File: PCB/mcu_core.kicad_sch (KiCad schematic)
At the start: 11 parts

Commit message: task: write matched LCSC part numbers into the schematic
Adds scripts/apply_lcsc_fields.py, which clones each symbol's existing
Manufacturer_Part_Number property (same indentation/effects) into a new
'LCSC' field with the matched code -- the field name the Fabrication
Toolkit plugin already installed in this repo recognizes for JLCPCB BOM
matching.

Applied the 31 confirmed matches from jlc_match.py across all sheets
(68 individual references). C_BUCK_OUT1 and R_ISET1 are left without an
LCSC field -- JLC doesn't stock those exact Yageo part numbers, to be
sorted out separately.

Verified: kicad-cli sch export bom round-trips every LCSC value
correctly, and ERC reports 0 violations.

Also switched jlc_match.py's BOM export to unranged references so each
match maps cleanly to individual schematic symbols.

Co-Authored-By: Claude Sonnet 5 <noreply@anthropic.com>
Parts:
- C_3V3_1: LCSC (none) -> C2936601
- C_3V3_2: LCSC (none) -> C131394
- C_3V3_3: LCSC (none) -> C106223
- R_BOOT_PU1, R_EN_PU1: LCSC (none) -> C60490
- R_USB_DM1, R_USB_DP1: LCSC (none) -> C138021
- R_VSYS1: LCSC (none) -> C114763
- R_VSYS2: LCSC (none) -> C60491
- SW_BOOT1: LCSC (none) -> C2915174
- U_MCU1: LCSC (none) -> C2913198
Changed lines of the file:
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@@
+			)
+		)
+		(property "LCSC" "C2936601"
+			(at 0 0 0)
+			(hide yes)
+			(show_name no)
+			(do_not_autoplace no)
+			(effects
+				(font
+					(size 1.27 1.27)
+				)
 			)
 		)
@@
 			)
 		)
+		(property "LCSC" "C2913198"
+			(at 0 0 0)
+			(hide yes)
+			(show_name no)
+			(do_not_autoplace no)
+			(effects
+				(font
+					(size 1.27 1.27)
+				)
+			)
+		)
 		(pin "1"
 		)
@@
 			)
 		)
+		(property "LCSC" "C60490"
+			(at 0 0 0)
+			(hide yes)
+			(show_name no)
+			(do_not_autoplace no)
+			(effects
+				(font
+					(size 1.27 1.27)
+				)
+			)
+		)
 		(pin "1"
 		)
@@
 			)
 		)
+		(property "LCSC" "C106223"
+			(at 0 0 0)
+			(hide yes)
+			(show_name no)
+			(do_not_autoplace no)
+			(effects
+				(font
+					(size 1.27 1.27)
+				)
+			)
+		)
 		(pin "1"
 		)
@@
 			)
 		)
+		(property "LCSC" "C60490"
+			(at 0 0 0)
+			(hide yes)
+			(show_name no)
+			(do_not_autoplace no)
+			(effects
+				(font
+					(size 1.27 1.27)
+				)
+			)
+		)
 		(pin "1"
 		)
@@
 			)
 		)
+		(property "LCSC" "C114763"
+			(at 0 0 0)
+			(hide yes)
+			(show_name no)
+			(do_not_autoplace no)
+			(effects
+				(font
+					(size 1.27 1.27)
+				)
+			)
+		)
 		(pin "1"
 		)
@@
 			)
 		)
+		(property "LCSC" "C2915174"
+			(at 0 0 0)
+			(hide yes)
+			(show_name no)
+			(do_not_autoplace no)
+			(effects
+				(font
+					(size 1.27 1.27)
+				)
+			)
+		)
 		(property "MF" "Panasonic"
 			(at 0 0 0)
@@
 			)
 		)
+		(property "LCSC" "C138021"
+			(at 0 0 0)
+			(hide yes)
+			(show_name no)
+			(do_not_autoplace no)
+			(effects
+				(font
+					(size 1.27 1.27)
+				)
+			)
+		)
 		(pin "1"
 		)
@@
 			)
 		)
+		(property "LCSC" "C60491"
+			(at 0 0 0)
+			(hide yes)
+			(show_name no)
+			(do_not_autoplace no)
+			(effects
+				(font
+					(size 1.27 1.27)
+				)
+			)
+		)
 		(pin "1"
 		)
@@
 			)
 		)
+		(property "LCSC" "C131394"
+			(at 0 0 0)
+			(hide yes)
+			(show_name no)
+			(do_not_autoplace no)
+			(effects
+				(font
+					(size 1.27 1.27)
+				)
+			)
+		)
 		(pin "1"
 		)
@@
 			(at 0 0 0)
 			(hide yes)
+			(show_name no)
+			(do_not_autoplace no)
+			(effects
+				(font
+					(size 1.27 1.27)
+				)
+			)
+		)
+		(property "LCSC" "C138021"
+			(at 0 0 0)
+			(hide yes)

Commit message: task: alert on Basic-library alternatives during JLC part matching (#33)
* task: alert on Basic-library alternatives during JLC part matching

JLC's "Extended" library carries a per-unique-part setup fee on top of
unit price; "Basic" doesn't. That fee doesn't amortize well on a board
with many distinct low-quantity parts -- confirmed the hard way: our
first real JLCPCB assembly quote came back at $333.84 vs PCBWay's
~$190 for the same order, and all 33 of our matched parts were
Extended.

jlc_match.py now does a secondary search for a same-value/same-package
Basic-library part whenever the real match lands on Extended, and
flags it in the report (new BasicAlt column + a Status alert) rather
than silently leaving it. On the current board this surfaces 11
plausible Basic-library swaps (common resistor/cap values, and the
generic 1N4148W diode and 2N7002 MOSFET, which are industry-standard
parts many brands stock identically).

This is alert-only, same as the rest of this script -- it doesn't
touch the schematic. Spot-checked 4 of the 11 suggestions directly
against JLC's catalog to confirm value/package actually match, not
just a keyword hit.

Co-Authored-By: Claude Sonnet 5 <noreply@anthropic.com>

* fix: two correctness bugs in Basic-library alternative matching

1. find_basic_alternative() trusted the raw keyword-search hit without
   verifying the candidate's actual value -- JLC's fuzzy full-text search
   can return a wrong-value part that just shares digits (e.g. searching
   "100 0402" surfaced a 1kΩ resistor, EIA code "1001", as a false match
   for a 100Ω part). Now parses and compares the actual numeric value
   (with unit) before accepting a candidate; falls back to exact
   model-name matching for non-numeric values (generic diode/transistor
   part families like "1N4148W", "2N7002").

2. The new value parser's regex required the unit to be the first
   character of the string, but JLC resistor descriptions carry a
   Chinese prefix ("厚膜电阻 10kΩ ±1%" = "thi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
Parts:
- C_3V3_1: LCSC C2936601 -> C19702; MF Yageo -> Samsung Electro-Mechanics; Manufacturer_Part_Number CC0603KRX5R7BB106 -> CL10A106KP8NNNC
- C_3V3_2: LCSC C131394 -> C1525; MF Yageo -> Samsung Electro-Mechanics; Manufacturer_Part_Number CC0402KRX7R9BB104 -> CL05B104KO5NNNC
- R_BOOT_PU1, R_EN_PU1: LCSC C60490 -> C25744; MF Yageo -> UNI-ROYAL(Uniroyal Elec); Manufacturer_Part_Number RC0402FR-0710KL -> 0402WGF1002TCE
- R_VSYS1: LCSC C114763 -> C25764; MF Yageo -> UNI-ROYAL(Uniroyal Elec); Manufacturer_Part_Number RC0402FR-07200KL -> 0402WGF2003TCE
- R_VSYS2: LCSC C60491 -> C25741; MF Yageo -> UNI-ROYAL(Uniroyal Elec); Manufacturer_Part_Number RC0402FR-07100KL -> 0402WGF1003TCE
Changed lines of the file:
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@@
 			)
 		)
-		(property "MF" "Yageo"
-			(at 0 0 0)
-			(hide yes)
-			(show_name no)
-			(do_not_autoplace no)
-			(effects
-				(font
-					(size 1.27 1.27)
-				)
-			)
-		)
-		(property "Manufacturer_Part_Number" "CC0603KRX5R7BB106"
-			(at 0 0 0)
-			(hide yes)
-			(show_name no)
-			(do_not_autoplace no)
-			(effects
-				(font
-					(size 1.27 1.27)
-				)
-			)
-		)
-		(property "LCSC" "C2936601"
+		(property "MF" "Samsung Electro-Mechanics"
+			(at 0 0 0)
+			(hide yes)
+			(show_name no)
+			(do_not_autoplace no)
+			(effects
+				(font
+					(size 1.27 1.27)
+				)
+			)
+		)
+		(property "Manufacturer_Part_Number" "CL10A106KP8NNNC"
+			(at 0 0 0)
+			(hide yes)
+			(show_name no)
+			(do_not_autoplace no)
+			(effects
+				(font
+					(size 1.27 1.27)
+				)
+			)
+		)
+		(property "LCSC" "C19702"
 			(at 0 0 0)
 			(hide yes)
@@
 			)
 		)
-		(property "MF" "Yageo"
-			(at 0 0 0)
-			(hide yes)
-			(show_name no)
-			(do_not_autoplace no)
-			(effects
-				(font
-					(size 1.27 1.27)
-				)
-			)
-		)
-		(property "Manufacturer_Part_Number" "RC0402FR-0710KL"
-			(at 0 0 0)
-			(hide yes)
-			(show_name no)
-			(do_not_autoplace no)
-			(effects
-				(font
-					(size 1.27 1.27)
-				)
-			)
-		)
-		(property "LCSC" "C60490"
+		(property "MF" "UNI-ROYAL(Uniroyal Elec)"
+			(at 0 0 0)
+			(hide yes)
+			(show_name no)
+			(do_not_autoplace no)
+			(effects
+				(font
+					(size 1.27 1.27)
+				)
+			)
+		)
+		(property "Manufacturer_Part_Number" "0402WGF1002TCE"
+			(at 0 0 0)
+			(hide yes)
+			(show_name no)
+			(do_not_autoplace no)
+			(effects
+				(font
+					(size 1.27 1.27)
+				)
+			)
+		)
+		(property "LCSC" "C25744"
 			(at 0 0 0)
 			(hide yes)
@@
 			)
 		)
-		(property "MF" "Yageo"
-			(at 0 0 0)
-			(hide yes)
-			(show_name no)
-			(do_not_autoplace no)
-			(effects
-				(font
-					(size 1.27 1.27)
-				)
-			)
-		)
-		(property "Manufacturer_Part_Number" "RC0402FR-0710KL"
-			(at 0 0 0)
-			(hide yes)
-			(show_name no)
-			(do_not_autoplace no)
-			(effects
-				(font
-					(size 1.27 1.27)
-				)
-			)
-		)
-		(property "LCSC" "C60490"
+		(property "MF" "UNI-ROYAL(Uniroyal Elec)"
+			(at 0 0 0)
+			(hide yes)
+			(show_name no)
+			(do_not_autoplace no)
+			(effects
+				(font
+					(size 1.27 1.27)
+				)
+			)
+		)
+		(property "Manufacturer_Part_Number" "0402WGF1002TCE"
+			(at 0 0 0)
+			(hide yes)
+			(show_name no)
+			(do_not_autoplace no)
+			(effects
+				(font
+					(size 1.27 1.27)
+				)
+			)
+		)
+		(property "LCSC" "C25744"
 			(at 0 0 0)
 			(hide yes)
@@
 			)
 		)
-		(property "MF" "Yageo"
-			(at 0 0 0)
-			(hide yes)
-			(show_name no)
-			(do_not_autoplace no)
-			(effects
-				(font
-					(size 1.27 1.27)
-				)
-			)
-		)
-		(property "Manufacturer_Part_Number" "RC0402FR-07200KL"
-			(at 0 0 0)
-			(hide yes)
-			(show_name no)
-			(do_not_autoplace no)
-			(effects
-				(font
-					(size 1.27 1.27)
-				)
-			)
-		)
-		(property "LCSC" "C114763"
+		(property "MF" "UNI-ROYAL(Uniroyal Elec)"
+			(at 0 0 0)
+			(hide yes)
+			(show_name no)
+			(do_not_autoplace no)
+			(effects
+				(font
+					(size 1.27 1.27)
+				)
+			)
+		)
+		(property "Manufacturer_Part_Number" "0402WGF2003TCE"
+			(at 0 0 0)
+			(hide yes)
+			(show_name no)
+			(do_not_autoplace no)
+			(effects
+				(font
+					(size 1.27 1.27)
+				)
+			)
+		)
+		(property "LCSC" "C25764"
 			(at 0 0 0)
 			(hide yes)
@@
 			)
 		)
-		(property "MF" "Yageo"
-			(at 0 0 0)
-			(hide yes)
-			(show_name no)
-			(do_not_autoplace no)
-			(effects
-				(font
-					(size 1.27 1.27)
-				)
-			)
-		)
-		(property "Manufacturer_Part_Number" "RC0402FR-07100KL"
-			(at 0 0 0)
-			(hide yes)
-			(show_name no)
-			(do_not_autoplace no)
-			(effects
-				(font
-					(size 1.27 1.27)
-				)
-			)
-		)
-		(property "LCSC" "C60491"
+		(property "MF" "UNI-ROYAL(Uniroyal Elec)"
+			(at 0 0 0)
+			(hide yes)
+			(show_name no)
+			(do_not_autoplace no)
+			(effects
+				(font
+					(size 1.27 1.27)
+				)
+			)
+		)
+		(property "Manufacturer_Part_Number" "0402WGF1003TCE"
+			(at 0 0 0)
+			(hide yes)
+			(show_name no)
+			(do_not_autoplace no)
+			(effects
+				(font
+					(size 1.27 1.27)
+				)
+			)
+		)
+		(property "LCSC" "C25741"
 			(at 0 0 0)
 			(hide yes)
@@
 			)
 		)
-		(property "MF" "Yageo"
-			(at 0 0 0)
-			(hide yes)
-			(show_name no)
-			(do_not_autoplace no)
-			(effects
-				(font
-					(size 1.27 1.27)
-				)
-			)
-		)
-		(property "Manufacturer_Part_Number" "CC0402KRX7R9BB104"
-			(at 0 0 0)
-			(hide yes)
-			(show_name no)
-			(do_not_autoplace no)
-			(effects
-				(font
-					(size 1.27 1.27)
-				)
-			)
-		)
-		(property "LCSC" "C131394"
-			(at 0 0 0)
-			(hide yes)
+		(property "MF" "Samsung Electro-Mechanics"
+			(at 0 0 0)
+			(hide yes)
+			(show_name no)
+			(do_not_autoplace no)
+			(effects
+				(font
+					(size 1.27 1.27)
+				)
+			)
+		)
+		(property "Manufacturer_Part_Number" "CL05B104KO5NNNC"
+			(at 0 0 0)
+			(hide yes)
+			(show_name no)
+			(do_not_autoplace no)
+			(effects
+				(font
+					(size 1.27 1.27)
+				)
+			)
+		)
+		(property "LCSC" "C1525"
+			(at 0 0 0)
+			(hide yes)

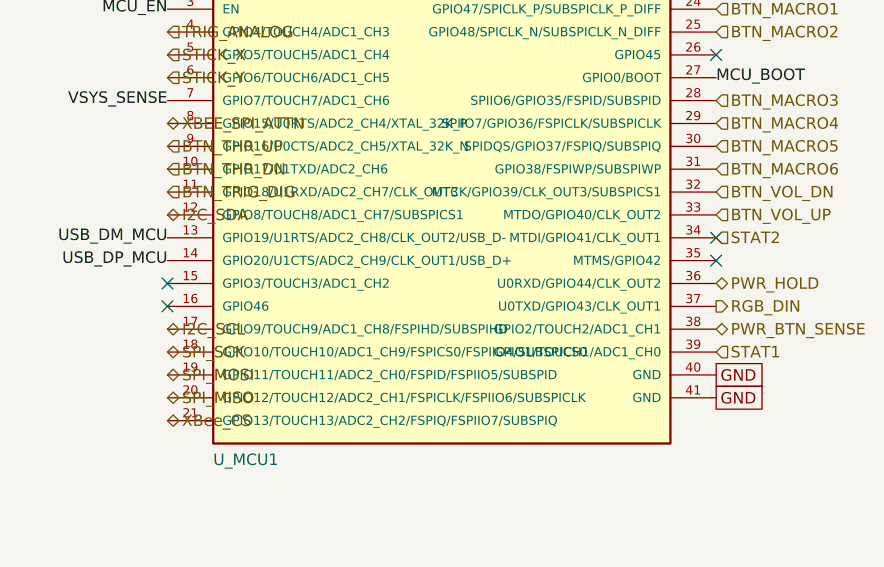
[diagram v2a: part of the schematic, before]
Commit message: Accelerometer-driven low-power mode (hardware, PCB only) (#47)
* feat: accelerometer-driven low-power mode (hardware, PCB 1/2)

Adds a QMA6100P accelerometer (I2C, shared OLED bus) and enables
host-commanded XBee pin-sleep, laying the hardware groundwork for a
low-power mode: OLED off + XBee sleep after a short idle timeout (no
buttons, no motion), full soft-latch power-off after a longer one.

- QMA6100P chosen after checking JLCPCB's actual parts library: no
  candidate accelerometer is Basic-library, so it won on price, size,
  and standby current (500nA), which matters since it has to watch for
  motion through the whole low-power period.
- Hand-authored symbol + footprint (no existing library part) — pad
  geometry pulled from JLCPCB/LCSC's own EasyEDA component data
  (LCSC C2887190), not estimated from the datasheet's low-res drawing.
- New Accelerometer sheet, wired into the existing I2C bus and into a
  new GPIO46 (INT1) interrupt line so the MCU can light-sleep instead
  of polling for wake conditions.
- XBee DTR moved off its permanent GND tie onto GPIO42 (SLEEP_RQ), so
  firmware can actually request/cancel pin-sleep instead of the radio
  being forced awake at all times.
- Placed, routed, DRC- and ERC-clean.

Firmware (driver, low-power state machine) and production file
generation are follow-up work — this PR is hardware/schematic only.

Co-Authored-By: Claude Sonnet 5 <noreply@anthropic.com>

* feat: accelerometer-driven low-power mode (firmware, PCB 2/2)

Progressive-enhancement low-power mode: idle cascade through
full -> dim OLED -> OLED off -> XBee sleep (each stage independently
timed, capped by a configurable aggressiveness mode), plus an
independent auto-poweroff timer that fires regardless of mode.

- PowerManager (power_management.h/.cpp): pure, unit-tested state
  machine. Takes "did anything happen this tick" and current time,
  reports which tier to be in and a one-shot poweroff flag. No
  capability flags needed for progressive enhancemen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
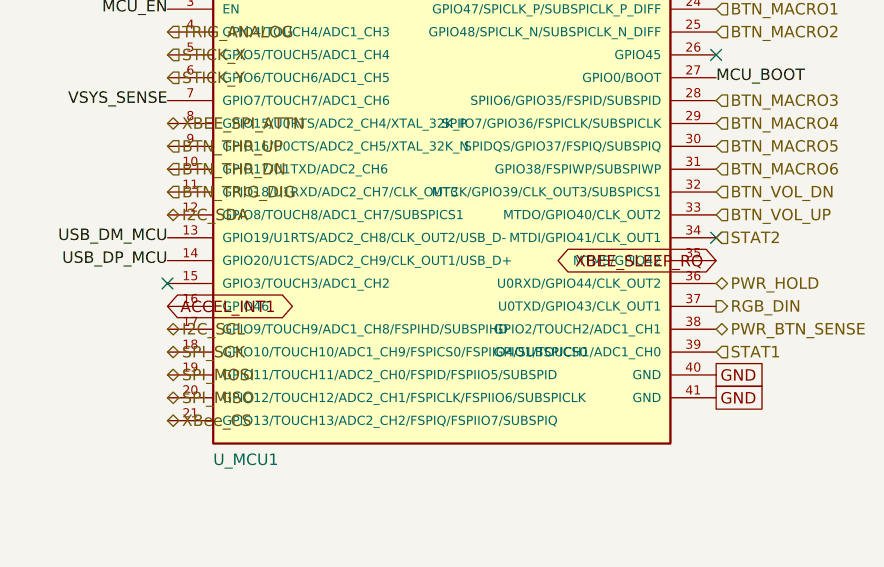
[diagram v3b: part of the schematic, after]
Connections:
- net ACCEL_INT1: now reaches U_MCU1.16 (GPIO46)
- net XBEE_SLEEP_RQ: now reaches U_MCU1.35 (MTMS/GPIO42)
- no-connect marks 5 -> 3
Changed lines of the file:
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@@
-	)
-	(no_connect
-		(at 237.49 99.06)
 	)
 	(no_connect
 		(at 237.49 96.52)
 	)
-	(no_connect
-		(at 176.53 104.14)
-	)
 	(label "MCU_BOOT"
 		(at 135.89 144.78 90)
@@
 		)
 	)
+	(global_label "XBEE_SLEEP_RQ"
+		(shape bidirectional)
+		(at 237.49 99.06 180)
+		(fields_autoplaced yes)
+		(effects
+			(font
+				(size 1.27 1.27)
+			)
+			(justify right)
+		)
+		(property "Intersheetrefs" "${INTERSHEET_REFS}"
+			(at 237.49 99.06 0)
+			(hide yes)
+			(show_name no)
+			(do_not_autoplace no)
+			(effects
+				(font
+					(size 1.27 1.27)
+				)
+			)
+		)
+	)
 	(global_label "GND"
 		(shape passive)
@@
 		(property "Intersheetrefs" "${INTERSHEET_REFS}"
 			(at 237.49 111.76 0)
+			(hide yes)
+			(show_name no)
+			(do_not_autoplace no)
+			(effects
+				(font
+					(size 1.27 1.27)
+				)
+			)
+		)
+	)
+	(global_label "ACCEL_INT1"
+		(shape bidirectional)
+		(at 176.53 104.14 0)
+		(fields_autoplaced yes)
+		(effects
+			(font
+				(size 1.27 1.27)
+			)
+			(justify left)
+		)
+		(property "Intersheetrefs" "${INTERSHEET_REFS}"
+			(at 176.53 104.14 0)
 			(hide yes)
 			(show_name no)
@@
 		)
 	)
+	(hierarchical_label "STAT2"
+		(shape input)
+		(at 237.49 96.52 0)
+		(effects
+			(font
+				(size 1.27 1.27)
+			)
+			(justify left)
+		)
+	)
 	(hierarchical_label "USB_DM"
 		(shape bidirectional)
@@
 		(effects
 			(font
-				(size 1.27 1.27)
-			)
-			(justify left)
-		)
-	)
-	(hierarchical_label "STAT2"
-		(shape input)
-		(at 237.49 96.52 0)
-		(effects
-			(font
